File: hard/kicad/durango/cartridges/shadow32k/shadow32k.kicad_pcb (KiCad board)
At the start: 2 copper layers, 74.9 x 63.5 mm, 10 parts, among them J1 to Computer, J2 SD Interface, U1 27/28C256, U2 62256, U4 74HC174, U5 74HC139, U6 74HC245, U7 74HC139

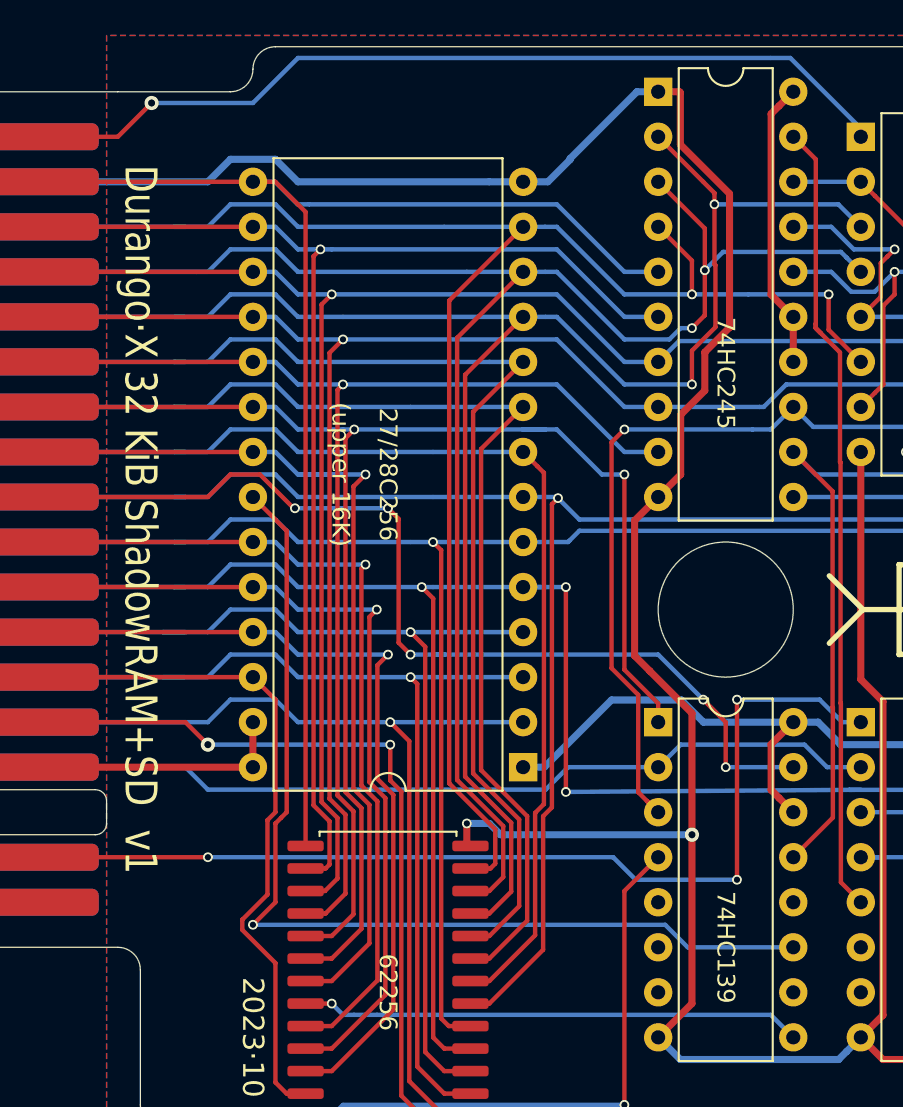
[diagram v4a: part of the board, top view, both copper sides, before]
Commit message: 32KiB enabled ShadowRAM
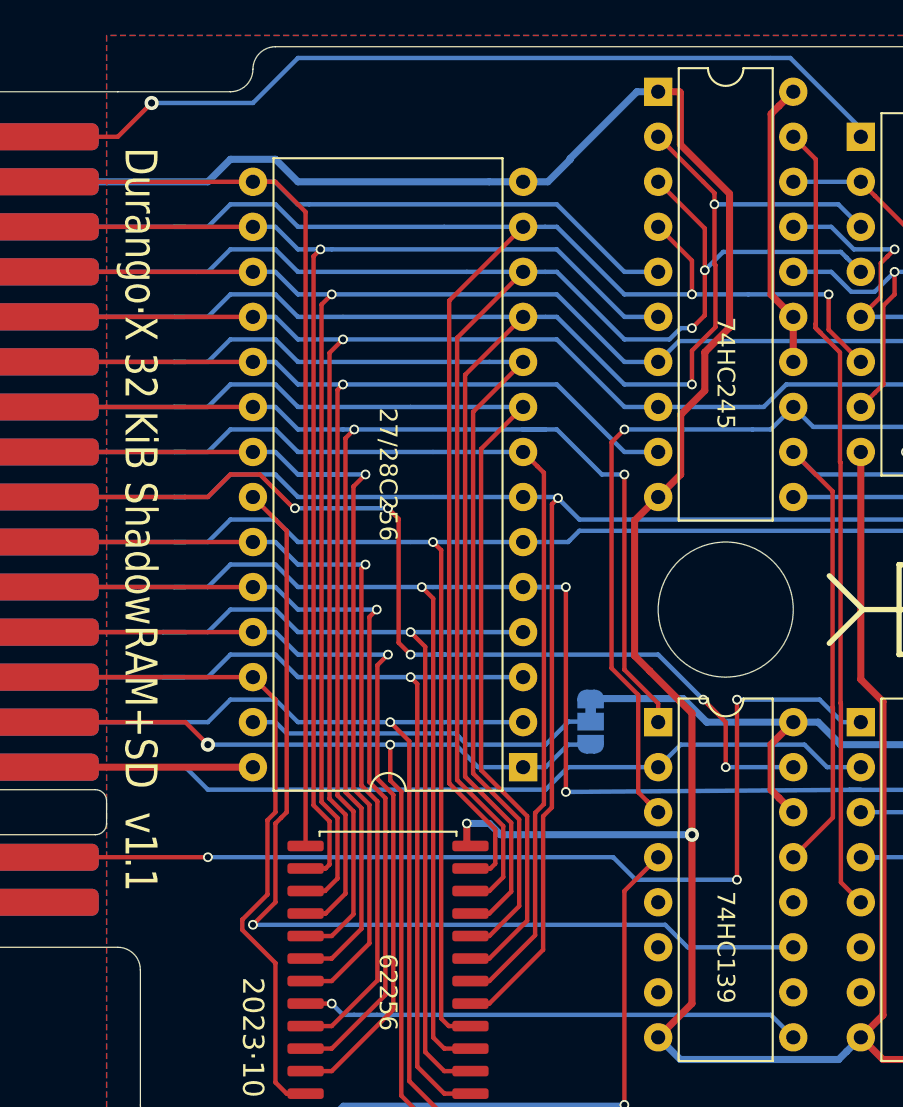
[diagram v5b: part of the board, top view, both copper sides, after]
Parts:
- added JP1: 32KiB, Jumper:SolderJumper-3_P1.3mm_Bridged12_RoundedPad1.0x1.5mm, B.Cu at (87.6, 110.5)
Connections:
- U1 pad 1: +5V -> A14
- U1 pad 27: +5V -> /MA14
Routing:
- net /MA14: track 0.00 -> 20.1 mm
- net A14: track 45.9 -> 58.3 mm
- net +5V: track 127.0 -> 119.1 mm
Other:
- board text added: "27C"
- board text added: "28C"
- board text added: "Durango·X 32 KiB ShadowRAM+SD v1.1"
- board text removed: "(upper 16K)"
- board text removed: "Durango·X 32 KiB ShadowRAM+SD v1"
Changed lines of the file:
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@@
   (general
     (thickness 1.6)
-    (drawings 42)
-    (tracks 681)
+    (drawings 43)
+    (tracks 693)
     (zones 0)
-    (modules 10)
-    (nets 43)
+    (modules 11)
+    (nets 44)
   )
   (page A4)
@@
   (net 41 /G~WE)
   (net 42 /~BL0)
+  (net 43 /MA14)
   (net_class Default "Esta es la clase de red por defecto."
     (clearance 0.2)
@@
     (uvia_drill 0.1)
     (add_net /G~WE)
+    (add_net /MA14)
     (add_net /MCLK)
     (add_net /MISO)
@@
     (add_net +5V)
     (add_net GND)
+  )
+  (module Jumper:SolderJumper-3_P1.3mm_Bridged12_RoundedPad1.0x1.5mm (layer B.Cu)
+    (at 87.63 110.46 270)
+    (descr "SMD Solder 3-pad Jumper, 1x1.5mm rounded Pads, 0.3mm gap, pads 1-2 bridged with 1 copper strip")
+    (tags "solder jumper open")
+    (attr virtual)
+    (fp_text reference JP1 (at 0.03 -1.905 unlocked) (layer B.SilkS)
+      (effects (font (size 0.8 0.7) (thickness 0.15)) (justify mirror))
+    )
+    (fp_text value 32KiB (at 5.11 0 unlocked) (layer B.SilkS)
+      (effects (font (size 1 1) (thickness 0.15)) (justify mirror))
+    )
+    (fp_poly (pts (xy -0.9 0.3) (xy -0.4 0.3) (xy -0.4 -0.3) (xy -0.9 -0.3)) (layer B.Cu) (width 0))
+    (fp_arc (start -1.35 0.3) (end -1.35 1) (angle 90) (layer B.SilkS) (width 0.12))
+    (fp_arc (start -1.35 -0.3) (end -2.05 -0.3) (angle 90) (layer B.SilkS) (width 0.12))
+    (fp_arc (start 1.35 -0.3) (end 1.35 -1) (angle 90) (layer B.SilkS) (width 0.12))
+    (fp_arc (start 1.35 0.3) (end 2.05 0.3) (angle 90) (layer B.SilkS) (width 0.12))
+    (fp_line (start 2.3 -1.25) (end -2.3 -1.25) (layer B.CrtYd) (width 0.05))
+    (fp_line (start 2.3 -1.25) (end 2.3 1.25) (layer B.CrtYd) (width 0.05))
+    (fp_line (start -2.3 1.25) (end -2.3 -1.25) (layer B.CrtYd) (width 0.05))
+    (fp_line (start -2.3 1.25) (end 2.3 1.25) (layer B.CrtYd) (width 0.05))
+    (fp_line (start -1.4 1) (end 1.4 1) (layer B.SilkS) (width 0.12))
+    (fp_line (start 2.05 0.3) (end 2.05 -0.3) (layer B.SilkS) (width 0.12))
+    (fp_line (start 1.4 -1) (end -1.4 -1) (layer B.SilkS) (width 0.12))
+    (fp_line (start -2.05 -0.3) (end -2.05 0.3) (layer B.SilkS) (width 0.12))
+    (fp_line (start -1.2 -1.2) (end -1.5 -1.5) (layer B.SilkS) (width 0.12))
+    (fp_line (start -1.5 -1.5) (end -0.9 -1.5) (layer B.SilkS) (width 0.12))
+    (fp_line (start -1.2 -1.2) (end -0.9 -1.5) (layer B.SilkS) (width 0.12))
+    (pad 1 smd custom (at -1.3 0 270) (size 1 0.5) (layers B.Cu B.Mask)
+      (net 4 +5V) (zone_connect 2)
+      (options (clearance outline) (anchor rect))
+      (primitives
+        (gr_circle (center 0 -0.25) (end 0.5 -0.25) (width 0))
+        (gr_circle (center 0 0.25) (end 0.5 0.25) (width 0))
+        (gr_poly (pts
+           (xy 0.55 0.75) (xy 0 0.75) (xy 0 -0.75) (xy 0.55 -0.75)) (width 0))
+      ))
+    (pad 2 smd rect (at 0 0 270) (size 1 1.5) (layers B.Cu B.Mask)
+      (net 43 /MA14))
+    (pad 3 smd custom (at 1.3 0 270) (size 1 0.5) (layers B.Cu B.Mask)
+      (net 29 A14) (zone_connect 2)
+      (options (clearance outline) (anchor rect))
+      (primitives
+        (gr_circle (center 0 -0.25) (end 0.5 -0.25) (width 0))
+        (gr_circle (center 0 0.25) (end 0.5 0.25) (width 0))
+        (gr_poly (pts
+           (xy -0.55 0.75) (xy 0 0.75) (xy 0 -0.75) (xy -0.55 -0.75)) (width 0))
+      ))
   )
   (module Connector_PinHeader_2.54mm:PinHeader_2x08_P2.54mm_Horizontal (layer F.Cu)
@@
       (net 1 GND))
     (pad 27 thru_hole oval (at 15.24 2.54 180) (size 1.6 1.6) (drill 0.8) (layers *.Cu *.Mask)
-      (net 4 +5V))
+      (net 43 /MA14))
     (pad 13 thru_hole oval (at 0 30.48 180) (size 1.6 1.6) (drill 0.8) (layers *.Cu *.Mask)
       (net 5 D2))
@@
       (net 19 D3))
     (pad 1 thru_hole rect (at 0 0 180) (size 1.6 1.6) (drill 0.8) (layers *.Cu *.Mask)
-      (net 4 +5V))
+      (net 29 A14))
     (model ${KISYS3DMOD}/Package_DIP.3dshapes/DIP-28_W15.24mm.wrl
       (at (xyz 0 0 0))
@@
     (pad 1 smd roundrect (at 45.72 -3.81 270) (size 1.524 8) (layers F.Cu F.Paste F.Mask) (roundrect_rratio 0.25))
   )
+  (gr_text 28C (at 87.63 107.315) (layer B.SilkS)
+    (effects (font (size 1 1) (thickness 0.2)) (justify mirror))
+  )
+  (gr_text 27C (at 87.63 113.665) (layer B.SilkS)
+    (effects (font (size 1 1) (thickness 0.2)) (justify mirror))
+  )
   (gr_text "GND\n\n ·\n\n+5V\n\n~CS~\n\nMOSI\n\nMCLK\n\nMISO\n\nGND" (at 118.745 88.9) (layer B.SilkS)
     (effects (font (size 0.77 0.77) (thickness 0.15)) (justify left mirror))
@@
   (gr_text 2023·10 (at 68.58 128.27 270) (layer F.SilkS)
     (effects (font (size 1.2 1.2) (thickness 0.2)))
-  )
-  (gr_text "(upper 16K)" (at 73.533 96.52 270) (layer F.SilkS)
-    (effects (font (size 1 1) (thickness 0.15)))
   )
   (gr_circle (center 82.55 133.985) (end 82.833981 133.985) (layer F.SilkS) (width 0.25))
@@
     (effects (font (size 1.8 1.8) (thickness 0.4)))
   )
-  (gr_text "Durango·X 32 KiB ShadowRAM+SD  v1" (at 62.23 99.06 270) (layer F.SilkS)
+  (gr_text "Durango·X 32 KiB ShadowRAM+SD  v1.1" (at 62.23 99.06 270) (layer F.SilkS)
     (effects (font (size 1.8 1.5) (thickness 0.3)))
   )
@@
   (via (at 93.98 109.22) (size 0.55) (drill 0.35) (layers F.Cu B.Cu) (net 3))
   (segment (start 95.25 110.49) (end 93.98 109.22) (width 0.25) (layer F.Cu) (net 3))
-  (segment (start 68.58 110.49) (end 68.58 113.03) (width 0.4) (layer F.Cu) (net 4))
   (segment (start 68.58 113.03) (end 55.88 113.03) (width 0.4) (layer F.Cu) (net 4))
   (segment (start 98.260001 114.770001) (end 99.06 115.57) (width 0.4) (layer F.Cu) (net 4))
@@
   (segment (start 114.3 82.55) (end 110.49 82.55) (width 0.4) (layer B.Cu) (net 4))
   (segment (start 116.84 85.09) (end 114.3 82.55) (width 0.4) (layer B.Cu) (net 4))
-  (segment (start 97.92863 110.49) (end 99.06 110.49) (width 0.4) (layer B.Cu) (net 4))
-  (segment (start 93.991998 110.49) (end 97.92863 110.49) (width 0.4) (layer B.Cu) (net 4))
-  (segment (start 92.741997 109.239999) (end 93.991998 110.49) (width 0.4) (layer B.Cu) (net 4))
-  (segment (start 88.810001 109.239999) (end 92.741997 109.239999) (width 0.4) (layer B.Cu) (net 4))
-  (segment (start 85.02 113.03) (end 88.810001 109.239999) (width 0.4) (layer B.Cu) (net 4))
-  (segment (start 83.82 113.03) (end 85.02 113.03) (width 0.4) (layer B.Cu) (net 4))
   (segment (start 115.65 109.14) (end 115.65 104.14) (width 0.4) (layer B.Cu) (net 4))
   (segment (start 114.3 110.49) (end 115.65 109.14) (width 0.4) (layer B.Cu) (net 4))
   (segment (start 110.49 110.49) (end 114.3 110.49) (width 0.4) (layer B.Cu) (net 4))
+  (segment (start 88.477592 109.16) (end 87.63 109.16) (width 0.4) (layer B.Cu) (net 4))
+  (segment (start 92.846998 109.16) (end 88.477592 109.16) (width 0.4) (layer B.Cu) (net 4))
+  (segment (start 94.176998 110.49) (end 92.846998 109.16) (width 0.4) (layer B.Cu) (net 4))
+  (segment (start 99.06 110.49) (end 94.176998 110.49) (width 0.4) (layer B.Cu) (net 4))
   (segment (start 85.07 82.55) (end 83.82 82.55) (width 0.25) (layer B.Cu) (net 5))
   (segment (start 71.12 82.55) (end 69.85 81.28) (width 0.25) (layer B.Cu) (net 5))
@@
   (segment (start 76.327 113.77931) (end 76.950091 114.402401) (width 0.25) (layer F.Cu) (net 29))
   (segment (start 76.327 111.76) (end 76.327 113.77931) (width 0.25) (layer F.Cu) (net 29))
+  (segment (start 76.327 111.76) (end 80.01 111.76) (width 0.25) (layer B.Cu) (net 29))
+  (segment (start 81.28 113.03) (end 83.82 113.03) (width 0.25) (layer B.Cu) (net 29))
+  (segment (start 80.01 111.76) (end 81.28 113.03) (width 0.25) (layer B.Cu) (net 29))
+  (segment (start 83.82 113.03) (end 85.09 113.03) (width 0.25) (layer B.Cu) (net 29))
+  (segment (start 85.09 113.03) (end 86.36 111.76) (width 0.25) (layer B.Cu) (net 29))
+  (segment (start 86.36 111.76) (end 87.63 111.76) (width 0.25) (layer B.Cu) (net 29))
   (via (at 66.04 118.11) (size 0.55) (drill 0.35) (layers F.Cu B.Cu) (net 30))
   (segment (start 55.88 118.11) (end 66.04 118.11) (width 0.25) (layer F.Cu) (net 30))
@@
   (segment (start 109.22 118.10859) (end 106.68141 115.57) (width 0.25) (layer B.Cu) (net 42))
   (segment (start 109.22 119.38) (end 109.22 118.10859) (width 0.25) (layer B.Cu) (net 42))
+  (segment (start 80.19499 111.30999) (end 80.196401 111.309991) (width 0.25) (layer B.Cu) (net 43))
+  (segment (start 80.64641 111.76) (end 85.09 111.76) (width 0.25) (layer B.Cu) (net 43))
+  (segment (start 80.196401 111.309991) (end 80.64641 111.76) (width 0.25) (layer B.Cu) (net 43))
+  (segment (start 80.01 111.125) (end 80.19499 111.30999) (width 0.25) (layer B.Cu) (net 43))
+  (segment (start 70.485 111.125) (end 80.01 111.125) (width 0.25) (layer B.Cu) (net 43))
+  (segment (start 86.39 110.46) (end 87.63 110.46) (width 0.25) (layer B.Cu) (net 43))
+  (segment (start 69.85 110.49) (end 70.485 111.125) (width 0.25) (layer B.Cu) (net 43))
+  (segment (start 85.09 111.76) (end 86.39 110.46) (width 0.25) (layer B.Cu) (net 43))
+  (segment (start 68.58 110.49) (end 69.85 110.49) (width 0.25) (layer B.Cu) (net 43))
   (zone (net 1) (net_name GND) (layer B.Cu) (hatch edge 0.508)
     (connect_pads (clearance 0.508))
